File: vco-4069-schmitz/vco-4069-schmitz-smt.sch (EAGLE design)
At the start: 46 parts, among them IC1 4069N, J1 22k pot (fp), J2 22k pot (fp), Q1 BC560, Q2 BC550B, Q3 BC550B

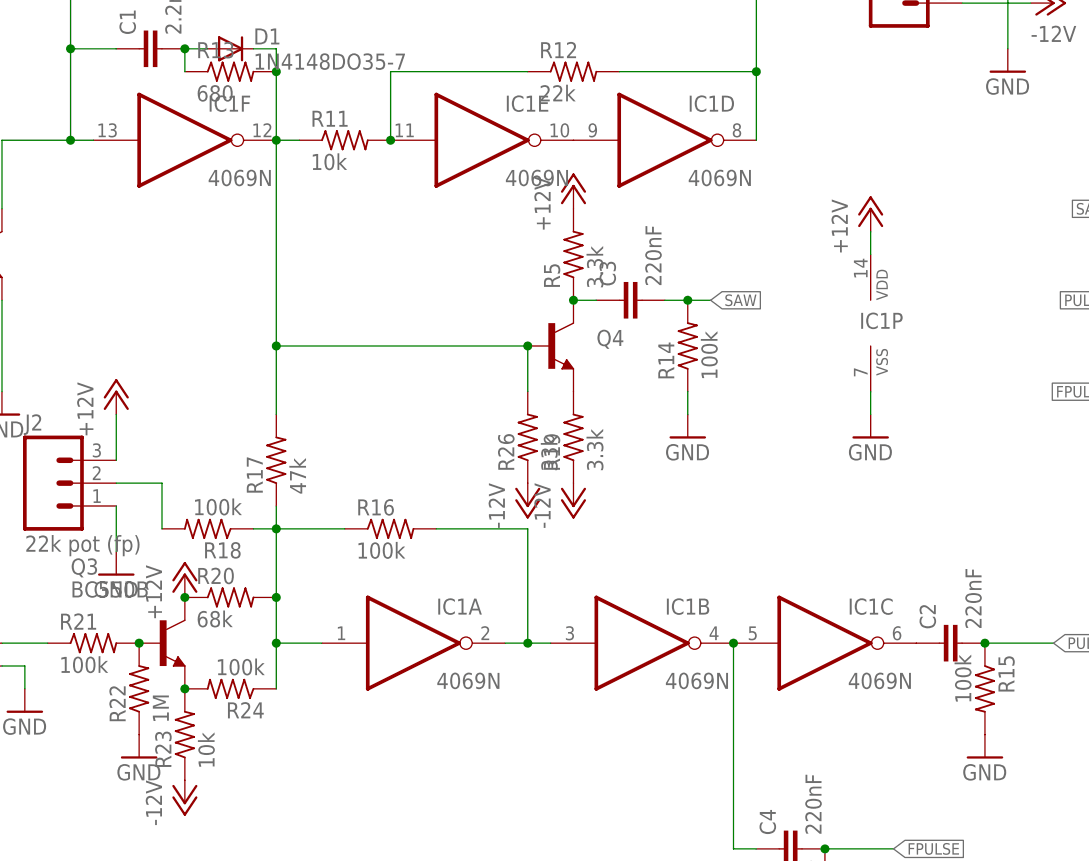
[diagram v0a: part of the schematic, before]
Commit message: through-hole 4069 vco
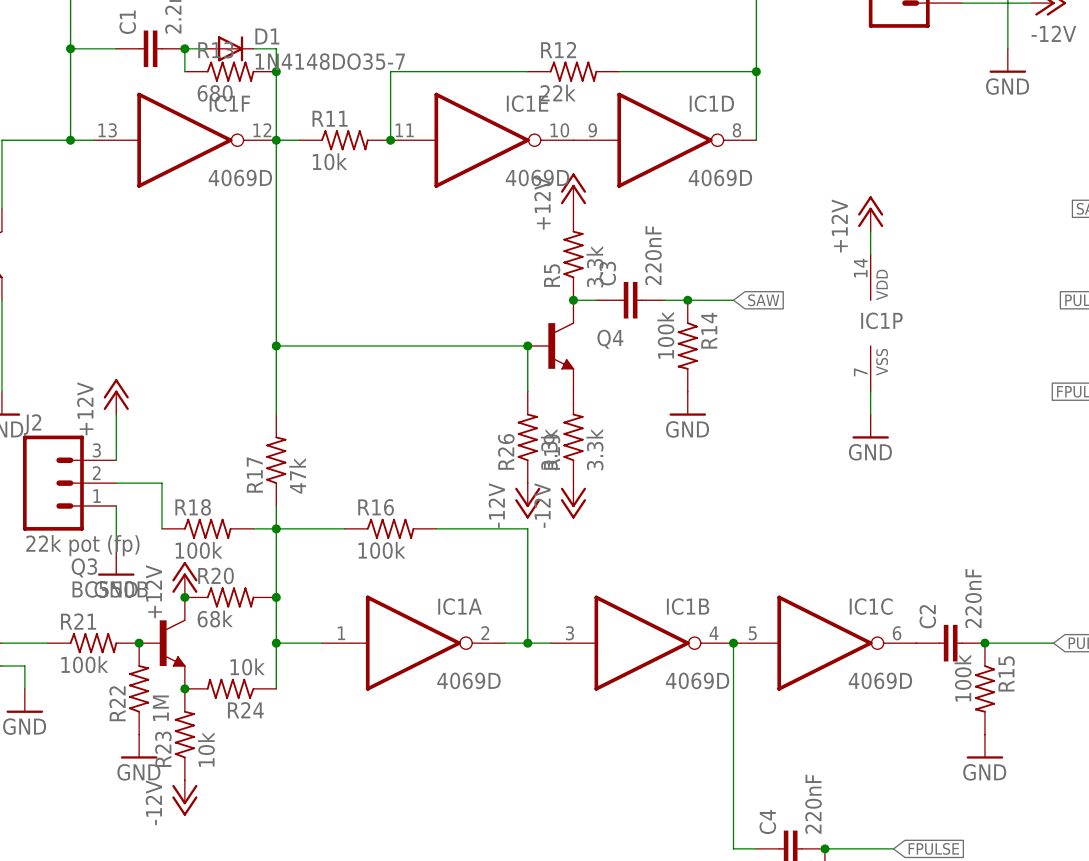
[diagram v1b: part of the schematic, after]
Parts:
- C1, C2, C3, C4: device resistor:C-EU025-025X050 -> resistor:C-EUC0805
- IC1: value 4069N -> 4069D; device 40xx:4069N -> 40xx:4069D
- Q4: device SparkFun-DiscreteSemi:TRANSISTOR_NPNBC547 -> SparkFun-DiscreteSemi:TRANSISTOR_NPNMMBT2222A
- R1, R10, R11, R12, R14, R15, R16, R17, R18, R19, R2, R20, R21, R22, R25, R5, R6, R9: device resistor:R-US_0207/2V -> resistor:R-US_R0805
- R13: device resistor:R-US_0204/7 -> resistor:R-US_R0805
- R23: device resistor:R-US_0207/5V -> resistor:R-US_R0805
- R24: value 100k -> 10k; device resistor:R-US_0207/2V -> resistor:R-US_R0805
- R26: value 33k -> 3.3k; device resistor:R-US_0207/2V -> resistor:R-US_R0805
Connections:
- net GND: now also R14.2; no longer R14.1
- net N$17: now also R18.2; no longer R18.1
- net N$18: now also R18.1; no longer R18.2
- net SAW: now also R14.1; no longer R14.2
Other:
- moved on the sheet: R14, R18
